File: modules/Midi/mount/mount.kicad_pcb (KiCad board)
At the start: 2 copper layers, 80.9 x 111.8 mm, 25 parts, among them J1 AudioJack2_SwitchT, J10 AudioJack2_SwitchT, J11 Conn_01x13_Male, J12 AudioJack2_SwitchT, J13 AudioJack2_SwitchT, J14 AudioJack2_SwitchT, J15 AudioJack2_SwitchT, J16 AudioJack2_SwitchT, J17 AudioJack2_SwitchT, J18 Conn_01x08_Female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

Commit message: update firmware
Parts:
- removed J16, J17: AudioJack2_SwitchT, elektrophon:Jack_3.5mm_QingPu_WQP-PJ398SM_Vertical_CircularHoles
- removed J18, J19: Conn_01x08_Female, Connector_PinHeader_2.54mm:PinHeader_1x08_P2.54mm_Vertical
- removed REF**: panel_5110_lcd, elektrophon:panel_5110_lcd
- removed SW1: Rotary_Encoder_Switch, 4ms-footprints:POT-9MM-ALPHA
- added D1: LED, LED_THT:LED_D5.0mm, F.Cu at (50.8, 45.7)
- added D2: POWER, LED_THT:LED_D5.0mm, F.Cu at (61.0, 45.7)
- added D3: CONNECT, LED_THT:LED_D5.0mm, F.Cu at (81.3, 45.7)
- added D4: Rx/Tx, LED_THT:LED_D5.0mm, F.Cu at (71.1, 45.7)
- J1, J2, J3, J4, J6, J7, J8, J9: footprint elektrophon:Jack_3.5mm_QingPu_WQP-PJ398SM_Vertical_CircularHoles -> elektrophon:Jack_3.5mm_WQP-PJ398SM_Vertical
- J10: value AudioJack2_SwitchT -> USB_B_Micro; footprint elektrophon:Jack_3.5mm_QingPu_WQP-PJ398SM_Vertical_CircularHoles -> Connector_USB:USB_Micro-B_Molex-105133-0031
- J11: value Conn_01x13_Male -> AudioJack2_SwitchT; footprint Connector_PinHeader_2.54mm:PinHeader_1x13_P2.54mm_Vertical -> elektrophon:Jack_3.5mm_WQP-PJ301BM_Vertical; moved to F.Cu
- J12, J13, J14: footprint elektrophon:Jack_3.5mm_QingPu_WQP-PJ398SM_Vertical_CircularHoles -> elektrophon:Jack_3.5mm_WQP-PJ301BM_Vertical
- J15: value AudioJack2_SwitchT -> Conn_01x13_Male; footprint elektrophon:Jack_3.5mm_QingPu_WQP-PJ398SM_Vertical_CircularHoles -> Connector_PinHeader_2.54mm:PinHeader_1x13_P2.54mm_Vertical
- J5: value AudioJack2_SwitchT -> BEAT; footprint elektrophon:Jack_3.5mm_QingPu_WQP-PJ398SM_Vertical_CircularHoles -> elektrophon:Jack_3.5mm_WQP-PJ398SM_Vertical
- moved J11 79.4 mm to (71.1, 121.9), turned to 0 degrees
- moved J3 55.9 mm to (50.8, 81.3)
- moved J15 54.3 mm to (101.6, 53.3), turned to 0 degrees
- moved J1 45.7 mm to (50.8, 61.0)
- moved J13 45.4 mm to (71.1, 81.3)
- moved J8 45.4 mm to (91.4, 81.3)
- moved J14 41.0 mm to (50.8, 142.2)
- moved J5 36.6 mm to (91.4, 61.0), turned to 0 degrees
- moved J6 36.6 mm to (71.1, 61.0), turned to 0 degrees
- moved J4 30.5 mm to (50.8, 121.9), turned to 0 degrees
- moved J10 30.5 mm to (91.4, 137.2), turned to 0 degrees
- moved J12 25.3 mm to (91.4, 122.1)
- moved J9 22.7 mm to (91.4, 101.6), turned to 0 degrees
- moved J2 20.3 mm to (50.8, 101.6)
- moved J7 5.08 mm to (71.1, 101.6), turned to 0 degrees
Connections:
- J1 pad T: Net-(J1-PadT) -> (no net)
- J1 pad TN: Net-(J1-PadTN) -> (no net)
- J12 pad T: Net-(J12-PadT) -> (no net)
- J13 pad T: Net-(J13-PadT) -> (no net)
- J14 pad T: Net-(J14-PadT) -> (no net)
- J2 pad T: Net-(J2-PadT) -> (no net)
- J2 pad TN: Net-(J2-PadTN) -> (no net)
- J3 pad T: Net-(J3-PadT) -> (no net)
- J3 pad TN: Net-(J3-PadTN) -> (no net)
- J4 pad T: Net-(J4-PadT) -> (no net)
- J4 pad TN: Net-(J4-PadTN) -> (no net)
- J5 pad T: Net-(J5-PadT) -> (no net)
- J5 pad TN: Net-(J5-PadTN) -> (no net)
- J6 pad T: Net-(J6-PadT) -> (no net)
- J6 pad TN: Net-(J6-PadTN) -> (no net)
- J7 pad T: Net-(J7-PadT) -> (no net)
- J7 pad TN: Net-(J7-PadTN) -> (no net)
- J8 pad T: Net-(J8-PadT) -> (no net)
- J8 pad TN: Net-(J8-PadTN) -> (no net)
- J9 pad T: Net-(J9-PadT) -> (no net)
- J9 pad TN: Net-(J9-PadTN) -> (no net)

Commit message: update schema
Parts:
- removed D3: CONNECT, LED_THT:LED_D5.0mm
- removed D4: Rx/Tx, LED_THT:LED_D5.0mm
- added J16: Conn_01x04_Male, Connector_PinHeader_2.54mm:PinHeader_1x04_P2.54mm_Vertical, F.Cu at (53.3, 139.7)
- added NT1: Net-Tie_2, NetTie:NetTie-2_THT_Pad1.0mm, F.Cu at (68.6, 147.3)
- added R1: 20, Resistor_THT:R_Axial_DIN0207_L6.3mm_D2.5mm_P10.16mm_Horizontal, F.Cu at (58.4, 152.4)
- added R2: 20, Resistor_THT:R_Axial_DIN0207_L6.3mm_D2.5mm_P10.16mm_Horizontal, F.Cu at (58.4, 157.5)
- added R3: 20, Resistor_THT:R_Axial_DIN0207_L6.3mm_D2.5mm_P10.16mm_Horizontal, F.Cu at (53.3, 135.9)
- added R4: 56, Resistor_THT:R_Axial_DIN0207_L6.3mm_D2.5mm_P10.16mm_Horizontal, F.Cu at (83.8, 157.5)
- added R5: 56, Resistor_THT:R_Axial_DIN0207_L6.3mm_D2.5mm_P10.16mm_Horizontal, F.Cu at (71.1, 157.5)
- D2: value POWER -> LED
- J1, J2, J3, J4, J6, J7, J8, J9: value AudioJack2_SwitchT -> INPUT
- J10: footprint Connector_USB:USB_Micro-B_Molex-105133-0031 -> Connector_USB:USB_Mini-B_Tensility_54-00023_Vertical
- J11, J12, J13, J14: value AudioJack2_SwitchT -> INPUT; footprint elektrophon:Jack_3.5mm_WQP-PJ301BM_Vertical -> elektrophon:Jack_3.5mm_WQP-PJ398SM_Vertical
- J15: value Conn_01x13_Male -> Conn_01x15_Male; footprint Connector_PinHeader_2.54mm:PinHeader_1x13_P2.54mm_Vertical -> Connector_PinHeader_2.54mm:PinHeader_1x15_P2.54mm_Vertical
- J5: value BEAT -> INPUT
- moved H1 117.3 mm to (53.3, 160.0)
- moved H2 116.7 mm to (108.9, 53.3)
- moved D1 107.6 mm to (86.4, 147.3)
- moved D2 102.4 mm to (73.7, 147.3)
- moved J5 87.0 mm to (101.6, 147.3)
- moved H3 66.4 mm to (53.3, 53.3)
- moved J11 63.7 mm to (101.6, 66.0)
- moved J14 53.0 mm to (101.6, 127.0)
- moved J13 39.7 mm to (101.6, 106.7)
- moved J12 37.1 mm to (101.6, 86.4)
- moved J10 32.1 mm to (61.0, 147.3)
- moved J3 27.4 mm to (61.0, 106.7)
- moved J8 27.4 mm to (81.3, 106.7)
- moved J9 27.4 mm to (81.3, 127.0)
- moved J2 18.3 mm to (61.0, 86.4)
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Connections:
- D1 pad 1: (no net) -> Net-(D1-Pad1)
- D1 pad 2: (no net) -> LED_ACTIVITY
- D2 pad 1: (no net) -> Net-(D2-Pad1)
- D2 pad 2: (no net) -> LED_CONNECT
- J1 pad T: (no net) -> Note_1
- J10 pad 2: (no net) -> Net-(J10-Pad2)
- J10 pad 3: (no net) -> Net-(J10-Pad3)
- J10 pad 5: (no net) -> Net-(J10-Pad5)
- J11 pad T: (no net) -> Note_3
- J12 pad T: (no net) -> Velocity_3
- J13 pad T: (no net) -> PITCH_BEND_3
- J14 pad T: (no net) -> OUT_TRIGGER_3
- J15 pad 1: (no net) -> +5V
- J15 pad 10: (no net) -> PITCH_BEND_2
- J15 pad 11: (no net) -> PITCH_BEND_3
- J15 pad 12: (no net) -> OUT_TRIGGER_1
- J15 pad 13: GND -> OUT_TRIGGER_2
- J15 pad 2: (no net) -> GND
- J15 pad 3: (no net) -> Note_1
- J15 pad 4: (no net) -> Note_2
- J15 pad 5: (no net) -> Note_3
- J15 pad 6: (no net) -> Velocity_1
- J15 pad 7: (no net) -> Velocity_2
- J15 pad 8: (no net) -> Velocity_3
- J15 pad 9: (no net) -> PITCH_BEND_1
- J2 pad T: (no net) -> Velocity_1
- J3 pad T: (no net) -> PITCH_BEND_1
- J4 pad T: (no net) -> OUT_TRIGGER_1
- J5 pad T: (no net) -> OUT_CLOCK
- J6 pad T: (no net) -> Note_2
- J7 pad T: (no net) -> Velocity_2
- J8 pad T: (no net) -> PITCH_BEND_2
- J9 pad T: (no net) -> OUT_TRIGGER_2
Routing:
- net +5V: track 0.00 -> 112.8 mm
- net GND: track 0.00 -> 100.6 mm
- net OUT_TRIGGER_1: track 0.00 -> 78.7 mm
- net PITCH_BEND_1: track 0.00 -> 66.0 mm
- net OUT_CLOCK: track 0.00 -> 61.4 mm
- net Velocity_1: track 0.00 -> 56.6 mm
- net OUT_TRIGGER_2: track 0.00 -> 56.2 mm
- net Note_1: track 0.00 -> 51.4 mm
- net OUT_TRIGGER_3: track 0.00 -> 43.6 mm
- net PITCH_BEND_2: track 0.00 -> 43.5 mm
- net LED_ACTIVITY: track 0.00 -> 38.7 mm
- net Velocity_2: track 0.00 -> 35.2 mm
- net PITCH_BEND_3: track 0.00 -> 30.9 mm
- net Note_2: track 0.00 -> 30.0 mm
- net LED_CONNECT: track 0.00 -> 25.0 mm
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- added copper zone on B.Cu, net GND
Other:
- board size 80.9 x 111.8 mm -> 60.6 x 111.8 mm
- board text removed: "R01"
- board text removed: "X4046"
- board text removed: "elektrophon"

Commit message: update schema
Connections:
- J16 pad 3: /PA12 -> /PA11
- J16 pad 4: /PA11 -> /PA12
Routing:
- net /PA11: track 12.3 -> 15.8 mm
- net /PA12: track 19.6 -> 20.3 mm
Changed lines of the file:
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@@
     (thickness 1.6)
     (drawings 4)
-    (tracks 82)
+    (tracks 87)
     (zones 0)
     (modules 28)
@@
   )
   (setup
-    (last_trace_width 0.381)
+    (last_trace_width 0.25)
     (user_trace_width 0.381)
     (trace_clearance 0.2)
@@
     (add_net "Net-(D1-Pad1)")
     (add_net "Net-(D2-Pad1)")
+    (add_net "Net-(J1-PadTN)")
+    (add_net "Net-(J10-Pad1)")
     (add_net "Net-(J10-Pad2)")
     (add_net "Net-(J10-Pad3)")
+    (add_net "Net-(J10-Pad4)")
     (add_net "Net-(J10-Pad5)")
     (add_net "Net-(J10-Pad6)")
+    (add_net "Net-(J11-PadTN)")
+    (add_net "Net-(J12-PadTN)")
+    (add_net "Net-(J13-PadTN)")
+    (add_net "Net-(J14-PadTN)")
+    (add_net "Net-(J2-PadTN)")
+    (add_net "Net-(J3-PadTN)")
+    (add_net "Net-(J4-PadTN)")
+    (add_net "Net-(J5-PadTN)")
+    (add_net "Net-(J6-PadTN)")
+    (add_net "Net-(J7-PadTN)")
+    (add_net "Net-(J8-PadTN)")
+    (add_net "Net-(J9-PadTN)")
     (add_net Note_1)
     (add_net Note_2)
@@
     (fp_line (start -0.635 -1.27) (end 1.27 -1.27) (layer F.Fab) (width 0.1))
     (pad 4 thru_hole oval (at 0 7.62) (size 1.7 1.7) (drill 1) (layers *.Cu *.Mask)
+      (net 25 /PA12))
+    (pad 3 thru_hole oval (at 0 5.08) (size 1.7 1.7) (drill 1) (layers *.Cu *.Mask)
       (net 24 /PA11))
-    (pad 3 thru_hole oval (at 0 5.08) (size 1.7 1.7) (drill 1) (layers *.Cu *.Mask)
-      (net 25 /PA12))
     (pad 2 thru_hole oval (at 0 2.54) (size 1.7 1.7) (drill 1) (layers *.Cu *.Mask)
       (net 6 LED_CONNECT))
@@
   (segment (start 101.6 131.92) (end 108.044999 125.475001) (width 0.25) (layer F.Cu) (net 23) (status 10))
   (segment (start 108.044999 125.475001) (end 108.044999 92.615001) (width 0.25) (layer F.Cu) (net 23))
-  (segment (start 53.34 152.4) (end 58.42 157.48) (width 0.25) (layer F.Cu) (net 24) (status 20))
-  (segment (start 53.34 147.32) (end 53.34 152.4) (width 0.25) (layer F.Cu) (net 24) (status 10))
-  (segment (start 58.42 149.86) (end 53.34 144.78) (width 0.25) (layer F.Cu) (net 25) (status 20))
-  (segment (start 58.42 152.4) (end 58.42 149.86) (width 0.25) (layer F.Cu) (net 25) (status 10))
-  (segment (start 52.164999 143.604999) (end 53.34 144.78) (width 0.25) (layer F.Cu) (net 25) (status 20))
-  (segment (start 52.164999 137.065001) (end 52.164999 143.604999) (width 0.25) (layer F.Cu) (net 25))
-  (segment (start 53.34 135.89) (end 52.164999 137.065001) (width 0.25) (layer F.Cu) (net 25) (status 10))
+  (segment (start 57.620001 156.680001) (end 58.42 157.48) (width 0.25) (layer F.Cu) (net 24))
+  (segment (start 52.164999 151.224999) (end 57.620001 156.680001) (width 0.25) (layer F.Cu) (net 24))
+  (segment (start 52.164999 145.955001) (end 52.164999 151.224999) (width 0.25) (layer F.Cu) (net 24))
+  (segment (start 53.34 144.78) (end 52.164999 145.955001) (width 0.25) (layer F.Cu) (net 24))
+  (segment (start 57.28863 152.4) (end 58.42 152.4) (width 0.25) (layer F.Cu) (net 25))
+  (segment (start 57.217919 152.4) (end 57.28863 152.4) (width 0.25) (layer F.Cu) (net 25))
+  (segment (start 53.34 148.522081) (end 57.217919 152.4) (width 0.25) (layer F.Cu) (net 25))
+  (segment (start 53.34 147.32) (end 53.34 148.522081) (width 0.25) (layer F.Cu) (net 25))
+  (segment (start 52.540001 136.689999) (end 53.34 135.89) (width 0.25) (layer B.Cu) (net 25))
+  (segment (start 52.164999 146.144999) (end 52.164999 137.065001) (width 0.25) (layer B.Cu) (net 25))
+  (segment (start 52.164999 137.065001) (end 52.540001 136.689999) (width 0.25) (layer B.Cu) (net 25))
+  (segment (start 53.34 147.32) (end 52.164999 146.144999) (width 0.25) (layer B.Cu) (net 25))
   (zone (net 2) (net_name GND) (layer B.Cu) (hatch edge 0.508)
     (connect_pads (clearance 0.508))

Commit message: update schema
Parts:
- added REF**: elektrophon logo, elektrophon:elektrophon logo, F.Cu at (66.5, 54.2)
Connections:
- J16 pad 3: /PA11 -> /PA12
- J16 pad 4: /PA12 -> /PA11
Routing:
- net /PA11: track 15.8 -> 12.9 mm
- net /PA12: track 20.3 -> 19.6 mm
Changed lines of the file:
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@@
     (thickness 1.6)
     (drawings 4)
-    (tracks 87)
+    (tracks 85)
     (zones 0)
-    (modules 28)
+    (modules 29)
     (nets 26)
   )
@@
     (add_net "Net-(D1-Pad1)")
     (add_net "Net-(D2-Pad1)")
-    (add_net "Net-(J1-PadTN)")
-    (add_net "Net-(J10-Pad1)")
     (add_net "Net-(J10-Pad2)")
     (add_net "Net-(J10-Pad3)")
-    (add_net "Net-(J10-Pad4)")
     (add_net "Net-(J10-Pad5)")
     (add_net "Net-(J10-Pad6)")
-    (add_net "Net-(J11-PadTN)")
-    (add_net "Net-(J12-PadTN)")
-    (add_net "Net-(J13-PadTN)")
-    (add_net "Net-(J14-PadTN)")
-    (add_net "Net-(J2-PadTN)")
-    (add_net "Net-(J3-PadTN)")
-    (add_net "Net-(J4-PadTN)")
-    (add_net "Net-(J5-PadTN)")
-    (add_net "Net-(J6-PadTN)")
-    (add_net "Net-(J7-PadTN)")
-    (add_net "Net-(J8-PadTN)")
-    (add_net "Net-(J9-PadTN)")
     (add_net Note_1)
     (add_net Note_2)
@@
     (add_net Velocity_2)
     (add_net Velocity_3)
+  )
+  (module "elektrophon:elektrophon logo" locked (layer F.Cu)
+    (at 66.548 54.229)
+    (fp_text reference REF** (at 0 3.556) (layer F.SilkS) hide
+      (effects (font (size 1 1) (thickness 0.15)))
+    )
+    (fp_text value "elektrophon logo" (at 0 -3.048) (layer F.Fab) hide
+      (effects (font (size 1 1) (thickness 0.15)))
+    )
+    (fp_text user kontakt (at 8.84 1.02) (layer B.SilkS)
+      (effects (font (size 0.8 1) (thickness 0.15)) (justify left mirror))
+    )
+    (fp_text user R01 (at -8.83 1) (layer B.SilkS)
+      (effects (font (size 0.8 1) (thickness 0.15)) (justify right mirror))
+    )
+    (fp_text user elektrophon (at 0 -1.016) (layer B.SilkS)
+      (effects (font (size 1.5 2) (thickness 0.3) italic) (justify mirror))
+    )
+    (fp_text user R01 (at 8.8 1.02) (layer F.SilkS)
+      (effects (font (size 0.8 1) (thickness 0.15)) (justify right))
+    )
+    (fp_text user kontakt (at -8.88 1) (layer F.SilkS)
+      (effects (font (size 0.8 1) (thickness 0.15)) (justify left))
+    )
+    (fp_text user elektrophon (at 0 -1.016) (layer F.SilkS)
+      (effects (font (size 1.5 2) (thickness 0.3) italic))
+    )
   )
   (module Resistor_THT:R_Axial_DIN0207_L6.3mm_D2.5mm_P10.16mm_Horizontal (layer F.Cu)
@@
     (fp_line (start -0.635 -1.27) (end 1.27 -1.27) (layer F.Fab) (width 0.1))
     (pad 4 thru_hole oval (at 0 7.62) (size 1.7 1.7) (drill 1) (layers *.Cu *.Mask)
+      (net 24 /PA11))
+    (pad 3 thru_hole oval (at 0 5.08) (size 1.7 1.7) (drill 1) (layers *.Cu *.Mask)
       (net 25 /PA12))
-    (pad 3 thru_hole oval (at 0 5.08) (size 1.7 1.7) (drill 1) (layers *.Cu *.Mask)
-      (net 24 /PA11))
     (pad 2 thru_hole oval (at 0 2.54) (size 1.7 1.7) (drill 1) (layers *.Cu *.Mask)
       (net 6 LED_CONNECT))
@@
   (segment (start 101.6 131.92) (end 108.044999 125.475001) (width 0.25) (layer F.Cu) (net 23) (status 10))
   (segment (start 108.044999 125.475001) (end 108.044999 92.615001) (width 0.25) (layer F.Cu) (net 23))
-  (segment (start 57.620001 156.680001) (end 58.42 157.48) (width 0.25) (layer F.Cu) (net 24))
-  (segment (start 52.164999 151.224999) (end 57.620001 156.680001) (width 0.25) (layer F.Cu) (net 24))
-  (segment (start 52.164999 145.955001) (end 52.164999 151.224999) (width 0.25) (layer F.Cu) (net 24))
-  (segment (start 53.34 144.78) (end 52.164999 145.955001) (width 0.25) (layer F.Cu) (net 24))
-  (segment (start 57.28863 152.4) (end 58.42 152.4) (width 0.25) (layer F.Cu) (net 25))
-  (segment (start 57.217919 152.4) (end 57.28863 152.4) (width 0.25) (layer F.Cu) (net 25))
-  (segment (start 53.34 148.522081) (end 57.217919 152.4) (width 0.25) (layer F.Cu) (net 25))
-  (segment (start 53.34 147.32) (end 53.34 148.522081) (width 0.25) (layer F.Cu) (net 25))
-  (segment (start 52.540001 136.689999) (end 53.34 135.89) (width 0.25) (layer B.Cu) (net 25))
-  (segment (start 52.164999 146.144999) (end 52.164999 137.065001) (width 0.25) (layer B.Cu) (net 25))
-  (segment (start 52.164999 137.065001) (end 52.540001 136.689999) (width 0.25) (layer B.Cu) (net 25))
-  (segment (start 53.34 147.32) (end 52.164999 146.144999) (width 0.25) (layer B.Cu) (net 25))
+  (segment (start 53.34 148.522081) (end 53.34 147.32) (width 0.25) (layer F.Cu) (net 24))
+  (segment (start 53.34 153.53137) (end 53.34 148.522081) (width 0.25) (layer F.Cu) (net 24))
+  (segment (start 57.28863 157.48) (end 53.34 153.53137) (width 0.25) (layer F.Cu) (net 24))
+  (segment (start 58.42 157.48) (end 57.28863 157.48) (width 0.25) (layer F.Cu) (net 24))
+  (segment (start 58.42 149.86) (end 53.34 144.78) (width 0.25) (layer F.Cu) (net 25))
+  (segment (start 58.42 152.4) (end 58.42 149.86) (width 0.25) (layer F.Cu) (net 25))
+  (segment (start 52.164999 143.604999) (end 52.490001 143.930001) (width 0.25) (layer F.Cu) (net 25))
+  (segment (start 52.164999 137.065001) (end 52.164999 143.604999) (width 0.25) (layer F.Cu) (net 25))
+  (segment (start 52.490001 143.930001) (end 53.34 144.78) (width 0.25) (layer F.Cu) (net 25))
+  (segment (start 53.34 135.89) (end 52.164999 137.065001) (width 0.25) (layer F.Cu) (net 25))
   (zone (net 2) (net_name GND) (layer B.Cu) (hatch edge 0.508)
     (connect_pads (clearance 0.508))

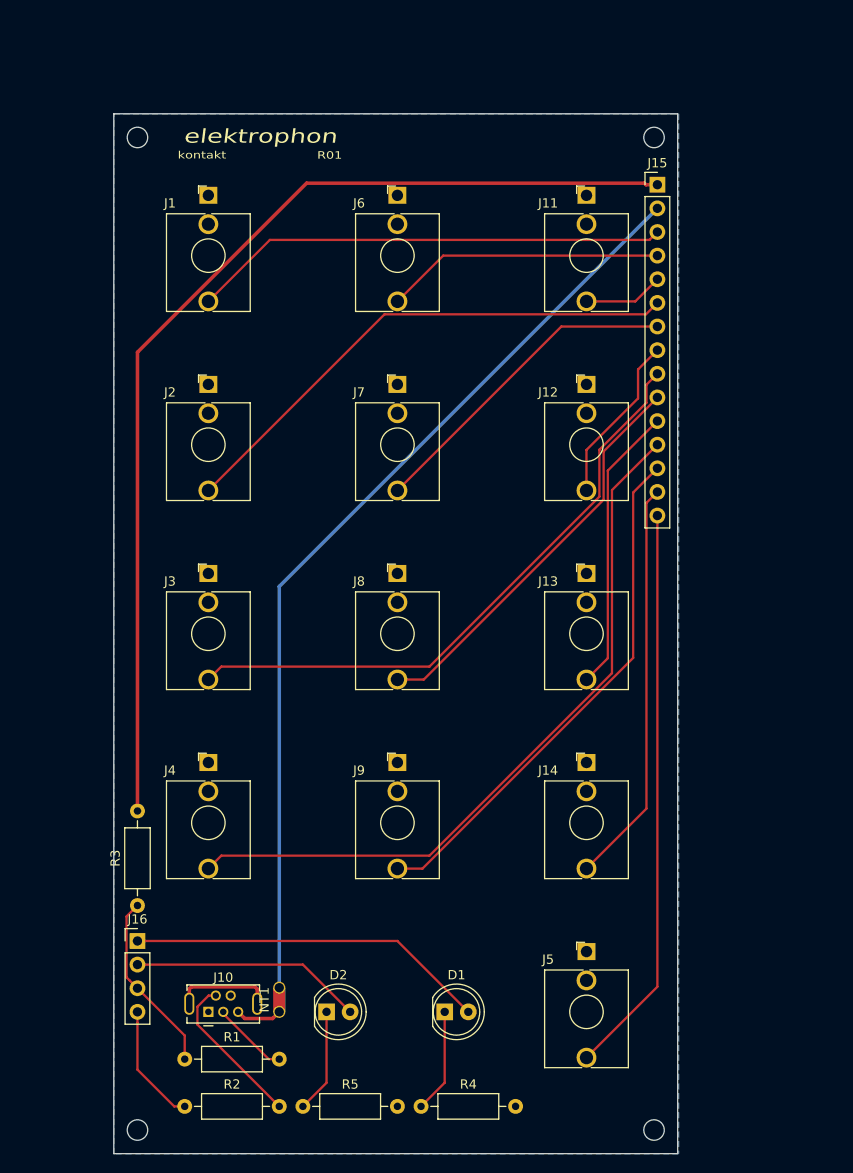
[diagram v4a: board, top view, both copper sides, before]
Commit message: reaname kontrast
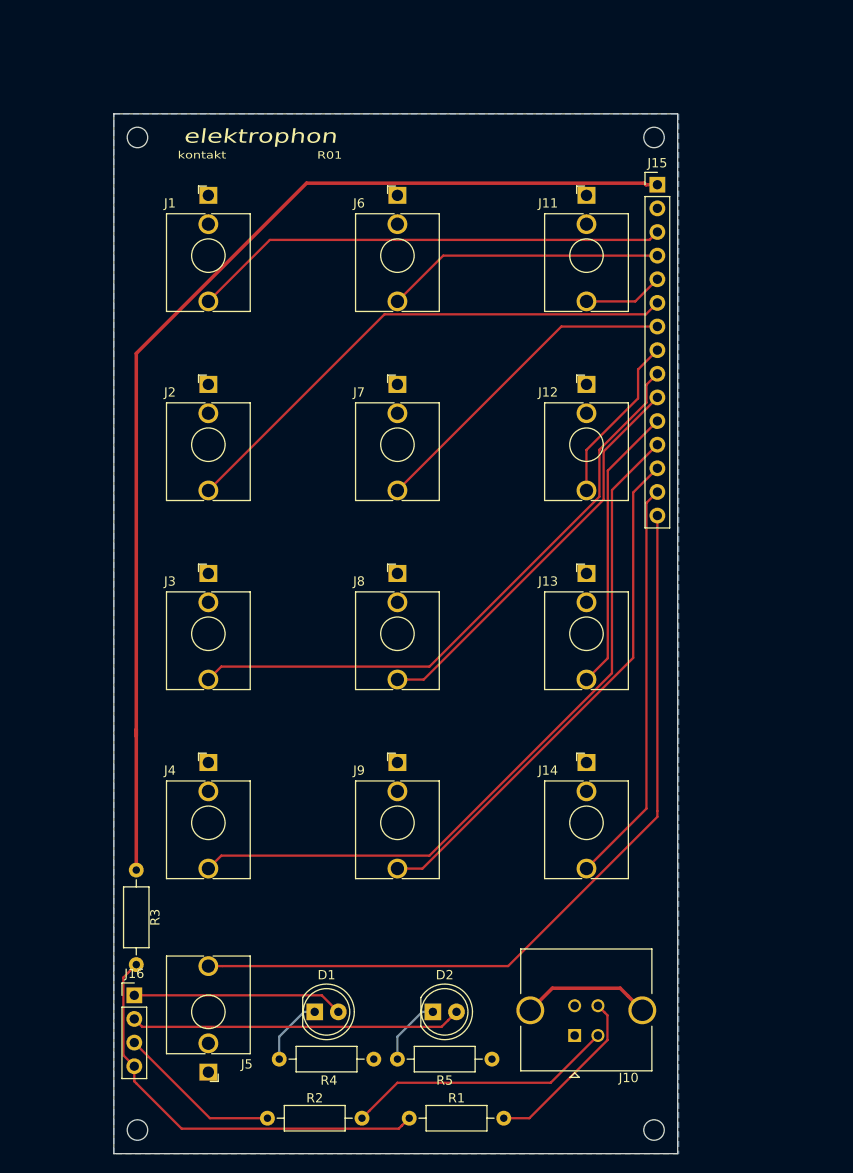
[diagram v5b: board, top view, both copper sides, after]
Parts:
- removed NT1: Net-Tie_2, NetTie:NetTie-2_THT_Pad1.0mm
- J10: value USB_B_Micro -> USB_B; footprint Connector_USB:USB_Mini-B_Tensility_54-00023_Vertical -> elektrophon:USB_B_TE_5787834_Vertical
- moved J5 40.6 mm to (61.0, 147.3), turned to 180 degrees
- moved J10 39.5 mm to (100.3, 149.9), turned to 180 degrees
- moved R1 25.0 mm to (82.5, 158.8)
- moved R4 16.1 mm to (68.6, 152.4)
- moved D1 14.0 mm to (72.4, 147.3)
- moved D2 11.4 mm to (85.1, 147.3)
- moved R5 11.4 mm to (81.3, 152.4)
- moved R2 8.98 mm to (67.3, 158.8)
- moved R3 6.35 mm to (53.2, 142.2)
- moved J16 5.85 mm to (53.0, 145.5)
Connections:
- J10 pad 4: (no net) -> GND
- J16 pad 3: /PA12 -> /PA11
- J16 pad 4: /PA11 -> /PA12
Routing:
- net GND: track 100.6 -> 0.00 mm
- net /PA12: track 19.6 -> 45.7 mm
- net OUT_CLOCK: track 61.4 -> 87.3 mm
- net LED_ACTIVITY: track 38.7 -> 22.7 mm
- net Net-(J10-Pad2): track 16.8 -> 29.0 mm
- net LED_CONNECT: track 25.0 -> 35.6 mm
- net Net-(J10-Pad6): track 10.7 -> 0.00 mm
- net Net-(J10-Pad3): track 8.24 -> 18.7 mm
- net Net-(J10-Pad5): track 5.01 -> 14.0 mm
- net +5V: track 112.8 -> 119.9 mm
- net /PA11: track 12.9 -> 17.7 mm
- net Net-(D1-Pad1): track 11.2 -> 7.33 mm
- net Net-(D2-Pad1): track 11.2 -> 7.33 mm
